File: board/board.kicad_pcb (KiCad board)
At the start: 2 copper layers, 50.8 x 33 mm, 78 parts, among them IC1 LVC245A, IC2 LVC245A, J1 Conn_01x06_Male, J10 Conn_01x02, J11 Conn_01x05_Male, J2 AudioJack4_Ground, J3 Conn_01x02, J5 Conn_01x01_Male, J6 Conn_01x01_Male, J7 Conn_01x01_Male, J8 Conn_01x01_Male, J9 Conn_01x01_Male, U1 THS7316, U2 10M02SCE144

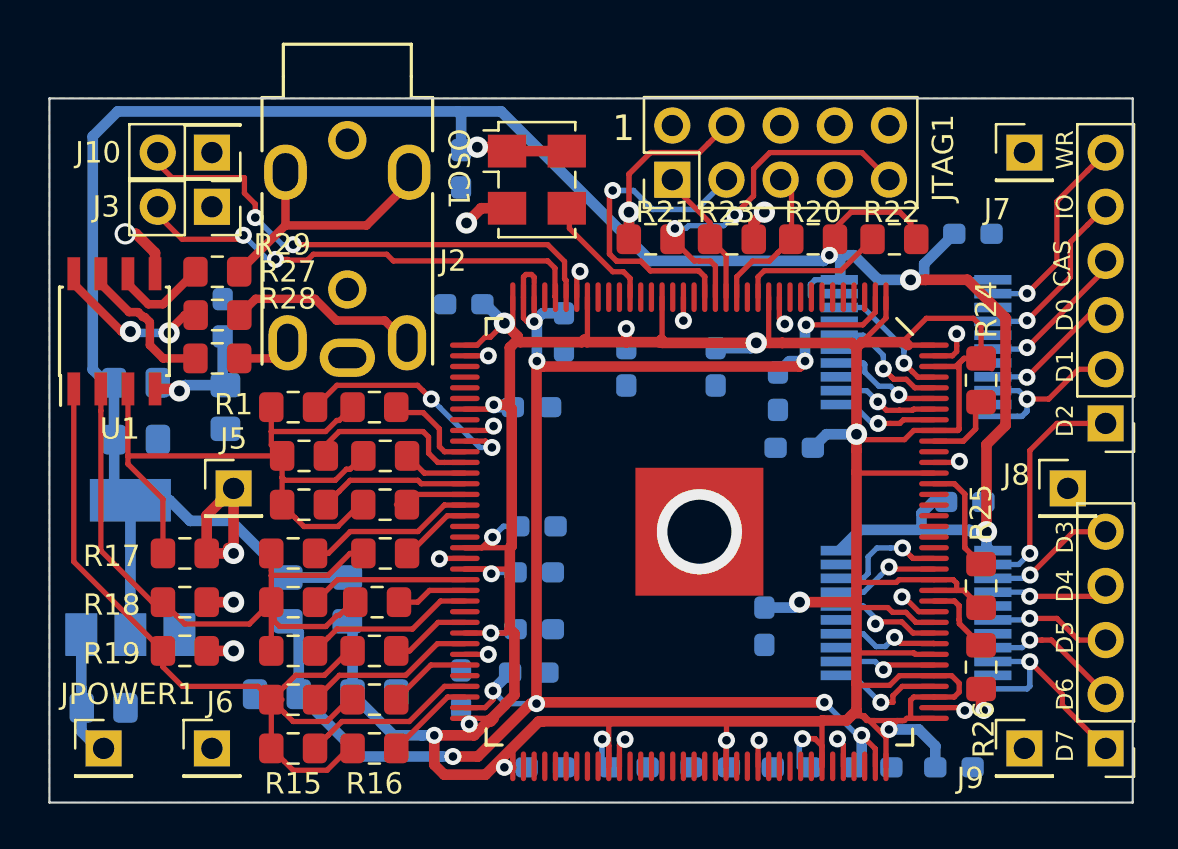
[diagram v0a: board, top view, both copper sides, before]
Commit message: Rework to be manufacturable by JLCPCB
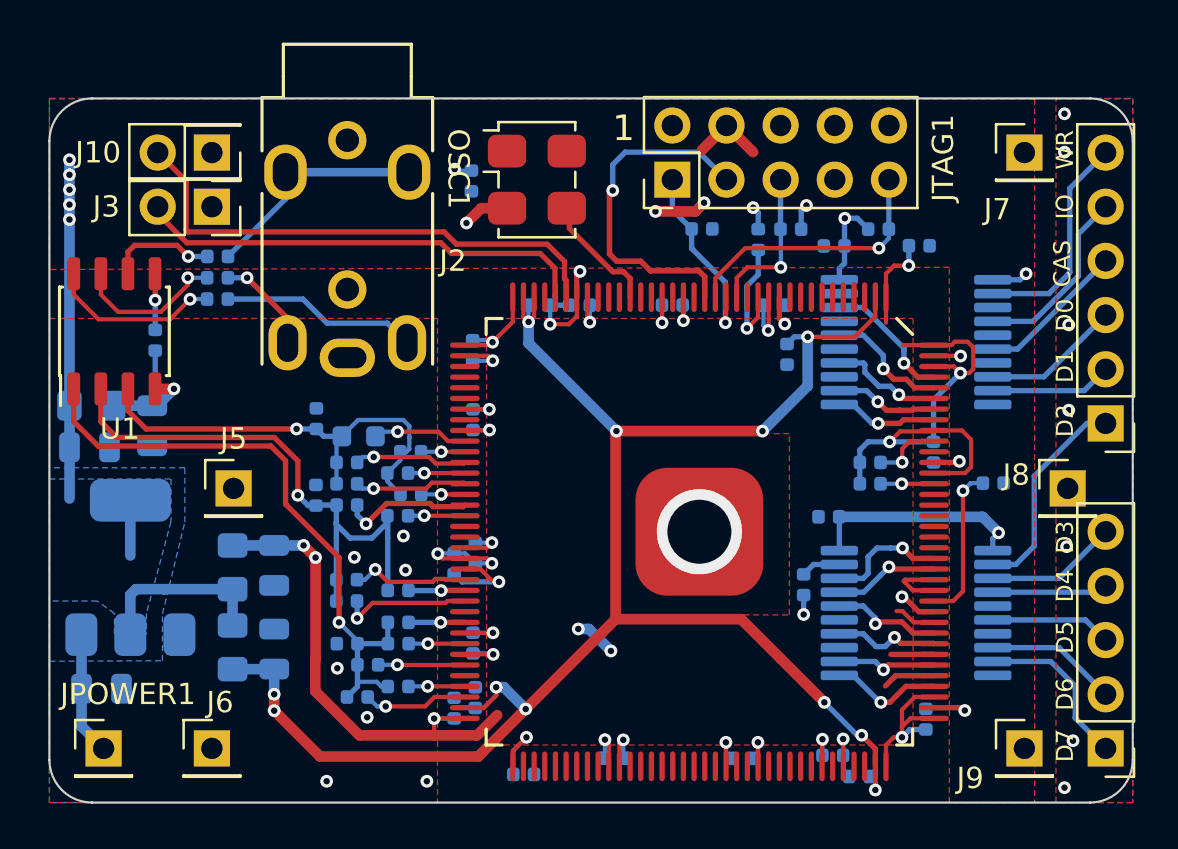
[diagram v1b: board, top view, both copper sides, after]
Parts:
- added C26: 100nF, Capacitor_SMD:C_0402_1005Metric, B.Cu at (218.6, 100.9)
- added C28: 100nF, Capacitor_SMD:C_0402_1005Metric, B.Cu at (211.8, 103.7)
- C1, C2, C3, C4, C5: footprint Capacitor_SMD:C_0805_2012Metric_Pad1.15x1.40mm_HandSolder -> Capacitor_SMD:C_0805_2012Metric
- C11, C12, C13, C14, C15, C16, C17, C18, C19, C20, C21, C22, C23, C24, C25, C31, C32, C33, C34, C6, C7, C8, C9: footprint Capacitor_SMD:C_0603_1608Metric_Pad1.05x0.95mm_HandSolder -> Capacitor_SMD:C_0402_1005Metric
- L1, L2, L3: footprint Capacitor_SMD:C_0805_2012Metric_Pad1.15x1.40mm_HandSolder -> Inductor_SMD:L_0805_2012Metric_Pad1.15x1.40mm_HandSolder
- R1: footprint Resistor_SMD:R_0805_2012Metric_Pad1.15x1.40mm_HandSolder -> Resistor_SMD:R_0603_1608Metric; moved to B.Cu
- R10, R11, R12, R13, R14, R15, R16, R17, R18, R19, R2, R20, R21, R22, R23, R24, R25, R26, R27, R28, R29, R3, R4, R5, R6, R7, R8, R9: footprint Resistor_SMD:R_0805_2012Metric_Pad1.15x1.40mm_HandSolder -> Resistor_SMD:R_0402_1005Metric; moved to B.Cu
- moved R21 10.7 mm to (216.7, 100.1)
- moved R17 8.83 mm to (190.3, 109.0), turned to 90 degrees
- moved R26 8.65 mm to (222.1, 112.0), turned to 180 degrees
- moved R18 7.93 mm to (190.3, 112.6), turned to 90 degrees
- moved C4 7.65 mm to (188.3, 115.9), turned to 270 degrees
- moved R19 7.62 mm to (191.8, 119.5), turned to 180 degrees
- moved R25 7.07 mm to (216.3, 112.0), turned to 0 degrees
- moved C11 6.54 mm to (219.3, 110.6), turned to 270 degrees
- moved C8 6.53 mm to (214.6, 100.9), turned to 180 degrees
- moved R24 6.47 mm to (216.3, 111.0), turned to 0 degrees
- moved C9 6.41 mm to (214.3, 113.6), turned to 0 degrees
- moved R22 6.38 mm to (211.0, 100.6), turned to 90 degrees
- moved R15 5.71 mm to (194.2, 121.6)
- moved L1 5.59 mm to (186.4, 116.0), turned to 270 degrees
- moved R13 5.58 mm to (194.2, 119.5)
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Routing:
- net /3V3B: track 209.6 -> 103.1 mm, vias 16 -> 22
- net /3V3A: track 137.3 -> 49.8 mm, vias 5 -> 11
- net Net-(R1-Pad2): track 33.7 -> 21.5 mm, vias 0 -> 1
- net Net-(R12-Pad2): track 37.7 -> 28.8 mm, vias 0 -> 1
- net Net-(R1-Pad1): track 11.3 -> 4.46 mm, vias 2 -> 1
- net GND: track 37.3 -> 43.4 mm, vias 22 -> 35
- net Net-(R15-Pad1): track 8.23 -> 2.65 mm, vias 0 -> 1
- net Net-(R13-Pad1): track 8.11 -> 2.63 mm, vias 0 -> 1
- net Net-(R10-Pad2): track 31.9 -> 26.9 mm, vias 0 -> 1
- net Net-(JTAG1-Pad9): track 17.3 -> 12.6 mm, vias 2 -> 1
- net Net-(R26-Pad2): track 3.55 -> 7.34 mm, vias 0 -> 1
- net /D1: track 9.11 -> 5.71 mm, vias 1 -> 0
- net /D7: track 11.0 -> 7.86 mm, vias 1 -> 0
- net Net-(R3-Pad1): track 8.34 -> 5.30 mm, vias 0 -> 1
- net /3V3C: track 86.1 -> 83.3 mm, vias 9 -> 11
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- added copper zone on B.Cu, net /3V3A
- added copper zone on F.Cu, net /3V3A
- added copper zone on F.Cu, net /3V3B
- added copper zone on F.Cu, net GND
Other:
- outline, holes or cut-outs redrawn
- net class Default: clearance 0.2 -> 0.15; via_dia 0.8 -> 0.6; via_drill 0.4 -> 0.3
- net class power: clearance 0.2 -> 0.15; via_dia 1 -> 0.6; via_drill 0.7 -> 0.3
- net class video: clearance 0.2 -> 0.15; via_dia 1 -> 0.6; via_drill 0.6 -> 0.3
- rule trace_clearance: 0.2 -> 0.15
- board text added: "ZX-Spectrum Component Video Rev. 2a (flatmush)"
- board text removed: "ZX-Spectrum Component Video Rev. 2"
